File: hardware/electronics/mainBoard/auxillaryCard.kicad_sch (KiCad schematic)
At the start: 0 parts

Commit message: added sheet
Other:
- title: (none) -> EPS Controller
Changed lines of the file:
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@@
 	(generator "eeschema")
 	(generator_version "9.0")
-	(paper "A4")
+	(paper "USLetter")
 	(title_block
+		(title "EPS Controller")
+		(date "2025-02-26")
 		(rev "1")
 		(comment 2 "PROTOTYPE")

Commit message: renamed sheet
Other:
- title: EPS Controller -> Auxillary M.2 Card
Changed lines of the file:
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@@
 	(paper "USLetter")
 	(title_block
-		(title "EPS Controller")
-		(date "2025-02-26")
+		(title "Auxillary M.2 Card")
+		(date "2025-03-03")
 		(rev "1")
 		(comment 2 "PROTOTYPE")

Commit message: added aux card hardware
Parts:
- added C127, C129, C131, C134: 100nF, lib_fp:MLCC0603, symbol lib_sch:C
- added C128, C89: 1uF, symbol lib_sch:C
- added C130, C132, C133: 100nF, symbol lib_sch:C
- added D13, D16, D17: ~, symbol lib_sch:LED
- added J12: Bus_M.2_Socket_E, symbol lib_sch:Bus_M.2_Socket_E
- added J6: M.2 Standoff, symbol lib_sch:Mounting-Hole
- added R80, R81, R84: 100R, symbol lib_sch:R
- added R82: 10K, symbol lib_sch:R_horizontal
- added R83: VAL, symbol lib_sch:R_horizontal
- added SW11, SW12: VAL, symbol .DS-Switches:SPDT
- added U21: TPS22996H-Q1, symbol lib_sch:TPS22996H-Q1
- added U22: TXS0104VxRUTR, symbol lib_sch:TXS0108EQWRKSRQ1
- added U23: TXS0104VxRUTR, lib_fp:RUT0012A, symbol lib_sch:TXS0104VxRUTR
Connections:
- new net: C129.1, SW12.2, U23.1 (VCCA)
- new net: D13.2, R80.1
- new net: D17.2, R84.1
- new net: C127.1, SW11.2, U22.2 (VCCA)
- new net: D16.2, R81.1
- new net: C130.1, U21.8 (VBIAS)
- new net +1V8: C89.1, U21.3 (VIN2)
- new net +3V3: C128.1, U21.2 (VIN1)
- new net AUX.GPIO1: U23.10 (B1)
- new net AUX.GPIO2: U23.9 (B2)
- new net AUX.GPIO3: U23.8 (B3)
- new net AUX.PWR_EN: R82.1, R83.1
- new net AUX.RST: J12.52 (~{PERST0})
- new net AUX_1V8: C132.1, SW11.3, SW12.3, U21.6 (VOUT2), U22.10 (OE), U23.12 (OE)
- new net AUX_CTS_1V8: J12.34 (UART_CTS), U22.4 (A3)
- new net AUX_GPIO1_1V8: J12.38 (VENDOR_DEFINED), U23.2 (A1)
- new net AUX_GPIO2_1V8: J12.40 (VENDOR_DEFINED), U23.3 (A2)
- new net AUX_GPIO3_1V8: J12.42 (VENDOR_DEFINED), U23.4 (A3)
- new net AUX_LED1: D16.1, J12.6 (~{LED_1})
- new net AUX_LED2: D13.1, J12.16 (~{LED_2})
- new net AUX_RTS_1V8: J12.36 (UART_RTS), U22.5 (A4)
- new net AUX_RXD_1V8: J12.22 (UART_RXD), U22.1 (A1)
- new net AUX_SCL_1V8: J12.60 (I2C_CLK), U22.7 (A6)
- new net AUX_SDA_1V8: J12.58 (I2C_DATA), U22.6 (A5)
- new net AUX_TXD_1V8: J12.32 (UART_TXD), U22.3 (A2)
- new net AUX_VDD: C131.1, C133.1, C134.1, D17.1, J12.2 (3.3V), J12.4 (3.3V), J12.72 (3.3V), J12.74 (3.3V), SW11.1, SW12.1, U21.7 (VOUT1), U22.19 (VCCB), U23.11 (VCCB)
- new net HUSB3.DM: J12.5 (USB_D-)
- new net HUSB3.DP: J12.3 (USB_D+)
- new net I2C4.SDA: U22.15 (B5)
- new net I2C4SCL: U22.14 (B6)
- new net ON1: R82.2, U21.1 (ON1)
- new net ON2: R83.2, U21.4 (ON2)
- new net USART6.CTS: U22.17 (B3)
- new net USART6.RTS: U22.16 (B4)
- new net USART6.RX: U22.18 (B2)
- new net USART6.TX: U22.20 (B1)
- new net VSS: C127.2, C128.2, C129.2, C130.2, C131.2, C132.2, C133.2, C134.2, C89.2, J12.1 (GND), J12.18 (GND), J12.33 (GND), J12.39 (GND), J12.45 (GND), J12.51 (GND), J12.57 (GND), J12.63 (GND), J12.69 (GND), J12.7 (GND), J12.75 (GND), J6.1, R80.2, R81.2, R84.2, U21.5 (GND), U22.11 (GND), U22.21 (GND_Pad), U23.6 (GND)
- no-connect marks 0 -> 44
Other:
- note added: "GPIO Voltage Selection"
- note added: "I2C/USART Voltage Selection"

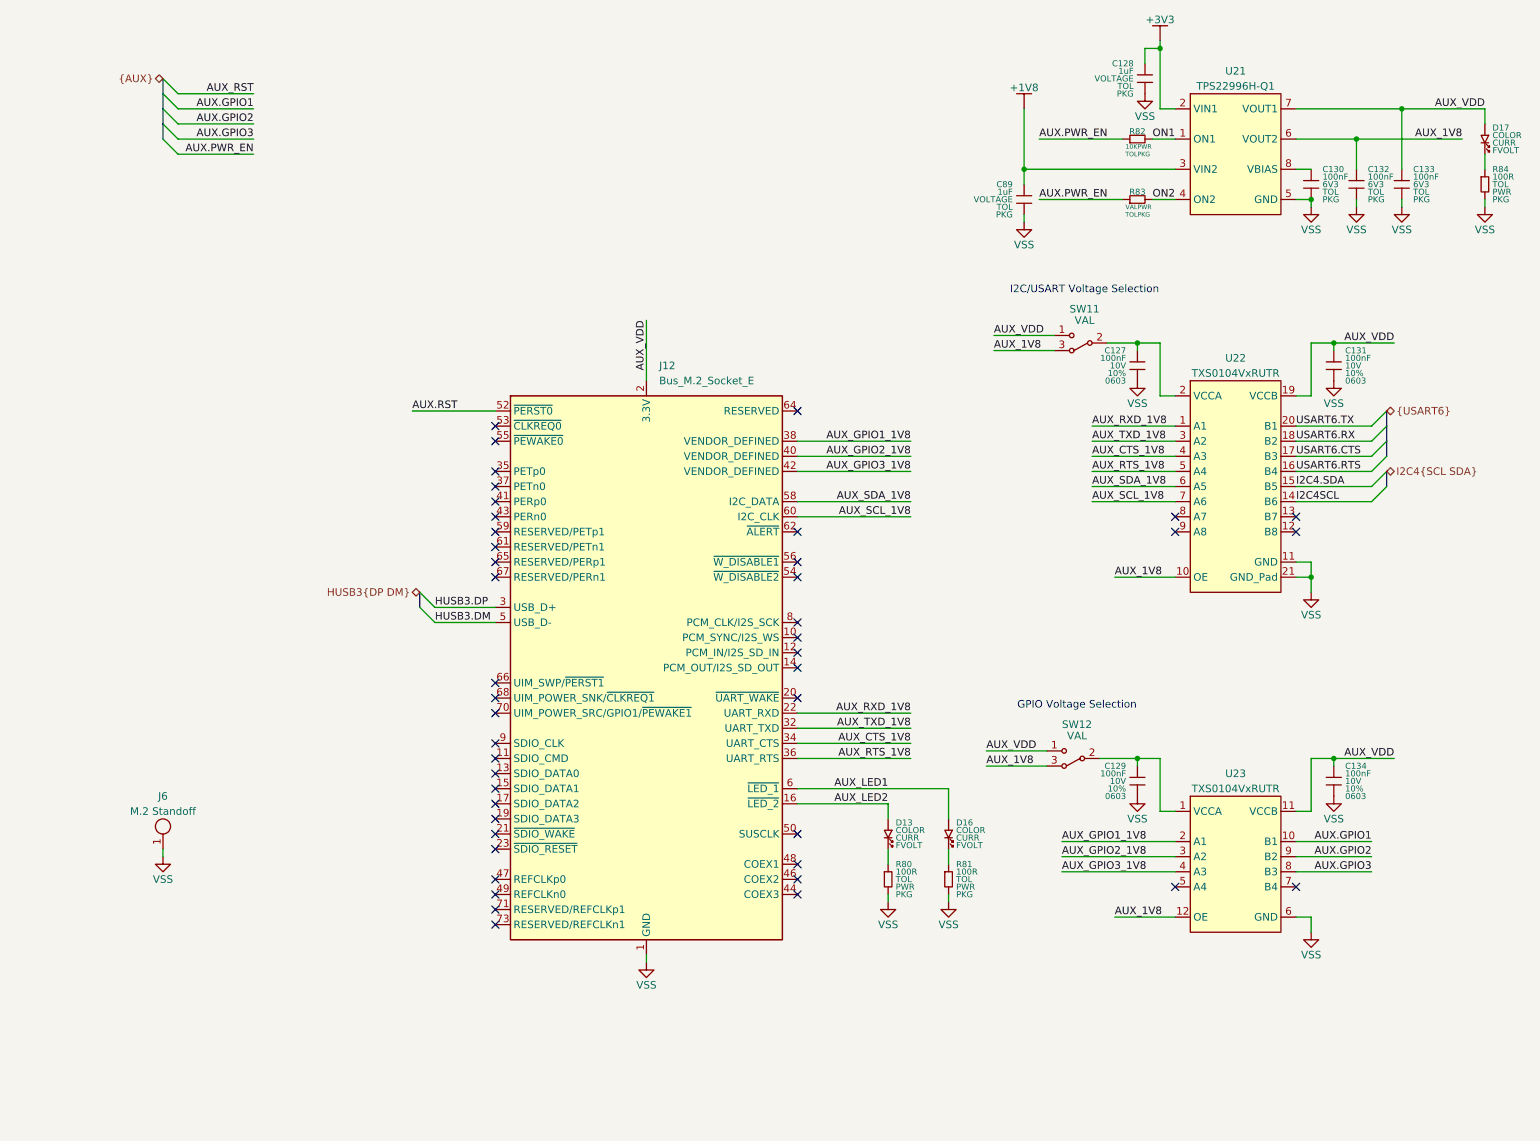
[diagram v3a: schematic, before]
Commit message: added components for aux card
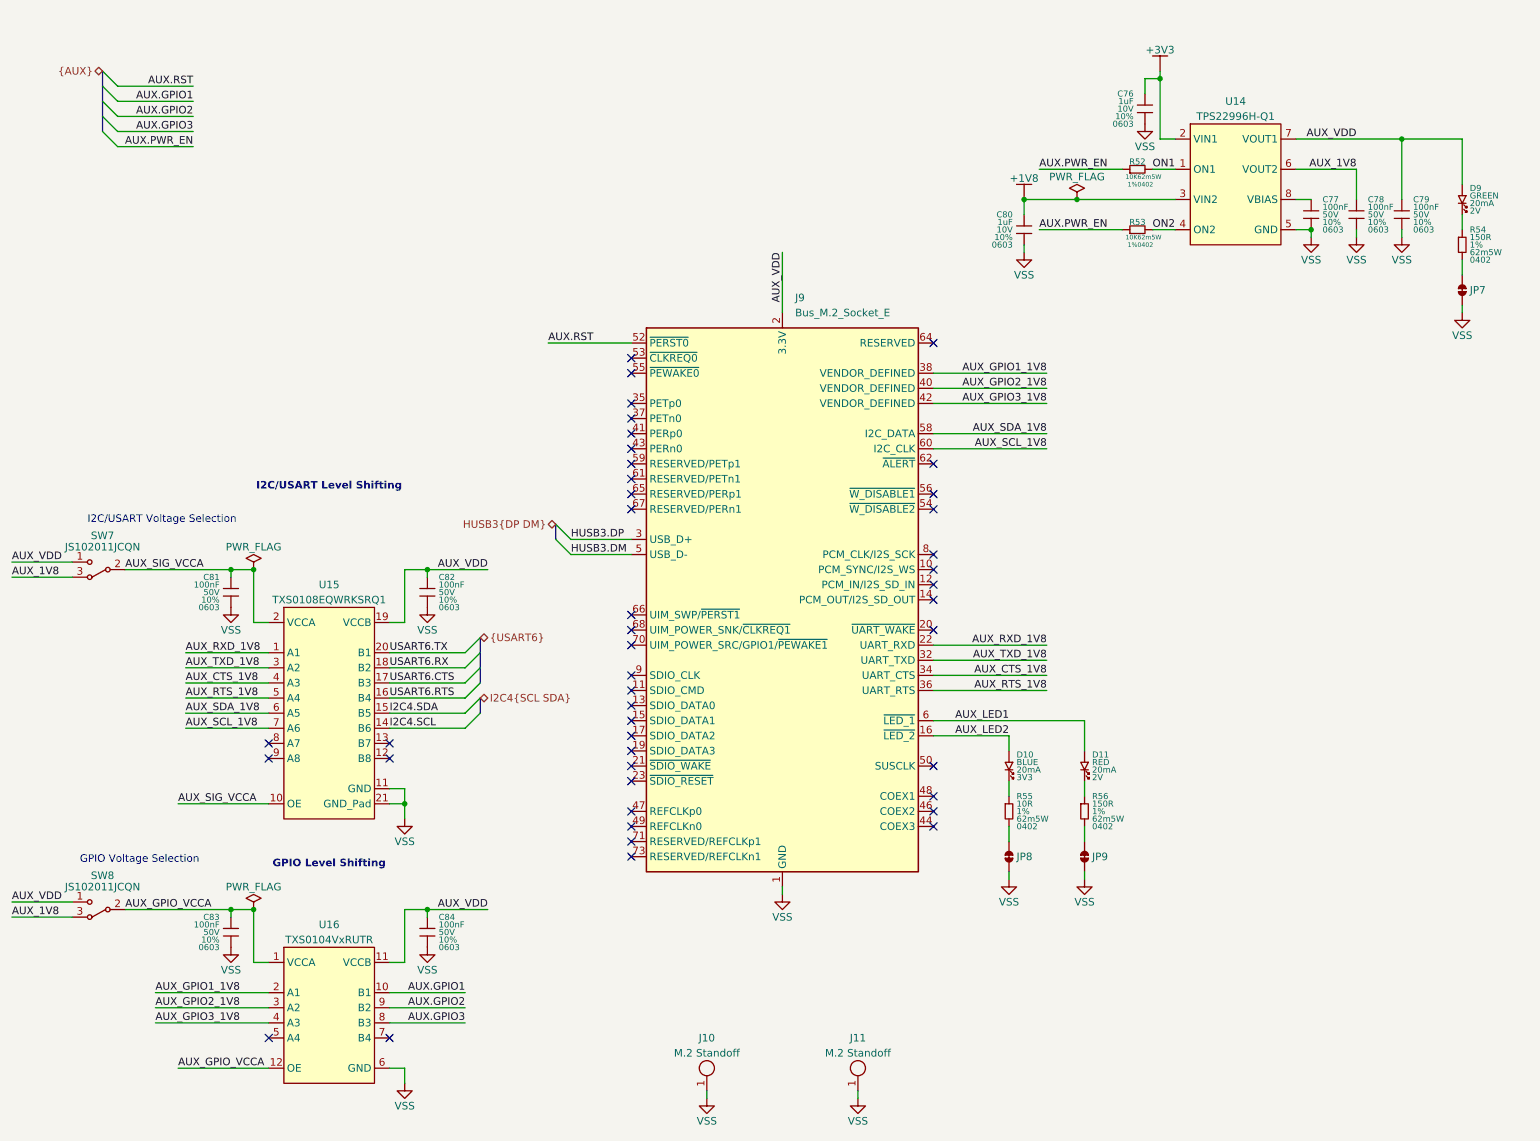
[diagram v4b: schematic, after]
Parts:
- removed C127, C129, C131, C134: 100nF, lib_fp:MLCC0603, symbol lib_sch:C
- removed C128, C89: 1uF, symbol lib_sch:C
- removed C130, C132, C133: 100nF, symbol lib_sch:C
- removed D13, D16, D17: ~, symbol lib_sch:LED
- removed J12: Bus_M.2_Socket_E, symbol lib_sch:Bus_M.2_Socket_E
- removed J6: M.2 Standoff, symbol lib_sch:Mounting-Hole
- removed R80, R81, R84: 100R, symbol lib_sch:R
- removed R82: 10K, symbol lib_sch:R_horizontal
- removed R83: VAL, symbol lib_sch:R_horizontal
- removed SW11, SW12: VAL, symbol .DS-Switches:SPDT
- removed U22: TXS0104VxRUTR, symbol lib_sch:TXS0108EQWRKSRQ1
- added C76, C80: 1uF, symbol lib_sch:C
- added C77, C78, C79, C81, C82, C83, C84: 100nF, symbol lib_sch:C
- added D10: LTST-C191TBKT, symbol lib_sch:LED
- added D11: LTST-C191KRKT, symbol lib_sch:LED
- added D9: LTST-C191KGKT, symbol lib_sch:LED
- added J10, J11: M.2 Standoff, symbol lib_sch:Mounting-Hole
- added J9: Bus_M.2_Socket_E, symbol lib_sch:Bus_M.2_Socket_E
- added JP7, JP8, JP9: ~, symbol lib_sch:Jumper_2_Bridged
- added R52, R53: 10K, symbol lib_sch:R_horizontal
- added R54, R56: 150R, symbol lib_sch:R
- added R55: 10R, symbol lib_sch:R
- added SW7, SW8: JS102011JCQN, symbol lib_sch:SPDT
- added U15: TXS0108EQWRKSRQ1, symbol lib_sch:TXS0108EQWRKSRQ1
- U16: renamed from U23; footprint lib_fp:RUT0012A -> (none)
- renumbered U21 to U14
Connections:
- net +1V8: now also C80.1
- net +3V3: now also C76.1
- net AUX.PWR_EN: now also R52.1, R53.1
- net AUX.RST: now also J9.52 (~{PERST0})
- net AUX_1V8: now also C78.1, SW7.3, SW8.3; no longer U16.12 (OE)
- net AUX_CTS_1V8: now also J9.34 (UART_CTS), U15.4 (A3)
- net AUX_GPIO1_1V8: now also J9.38 (VENDOR_DEFINED)
- net AUX_GPIO2_1V8: now also J9.40 (VENDOR_DEFINED)
- net AUX_GPIO3_1V8: now also J9.42 (VENDOR_DEFINED)
- net AUX_LED1: now also D11.1, J9.6 (~{LED_1})
- net AUX_LED2: now also D10.1, J9.16 (~{LED_2})
- net AUX_RTS_1V8: now also J9.36 (UART_RTS), U15.5 (A4)
- net AUX_RXD_1V8: now also J9.22 (UART_RXD), U15.1 (A1)
- net AUX_SCL_1V8: now also J9.60 (I2C_CLK), U15.7 (A6)
- net AUX_SDA_1V8: now also J9.58 (I2C_DATA), U15.6 (A5)
- net AUX_TXD_1V8: now also J9.32 (UART_TXD), U15.3 (A2)
- net AUX_VDD: now also C79.1, C82.1, C84.1, D9.1, J9.2 (3.3V), J9.4 (3.3V), J9.72 (3.3V), J9.74 (3.3V), SW7.1, SW8.1, U15.19 (VCCB)
- net HUSB3.DM: now also J9.5 (USB_D-)
- net HUSB3.DP: now also J9.3 (USB_D+)
- net I2C4.SDA: now also U15.15 (B5)
- net ON1: now also R52.2
- net ON2: now also R53.2
- net USART6.CTS: now also U15.17 (B3)
- net USART6.RTS: now also U15.16 (B4)
- net USART6.RX: now also U15.18 (B2)
- net USART6.TX: now also U15.20 (B1)
- net VSS: now also C76.2, C77.2, C78.2, C79.2, C80.2, C81.2, C82.2, C83.2, C84.2, J10.1, J11.1, J9.1 (GND), J9.18 (GND), J9.33 (GND), J9.39 (GND), J9.45 (GND), J9.51 (GND), J9.57 (GND), J9.63 (GND), J9.69 (GND), J9.7 (GND), J9.75 (GND), JP7.2, JP8.2, JP9.2, U15.11 (GND), U15.21 (GND_Pad)
- net AUX_GPIO_VCCA: now reaches U16.1 (VCCA)
- net AUX_GPIO_VCCA: now also U16.12 (OE), C83.1, SW8.2
- net at U14.8 (VBIAS): now also C77.1
- new net: D10.2, R55.1
- new net: JP8.1, R55.2
- new net: D9.2, R54.1
- new net: JP9.1, R56.2
- new net: JP7.1, R54.2
- new net: D11.2, R56.1
- new net AUX_SIG_VCCA: C81.1, SW7.2, U15.10 (OE), U15.2 (VCCA)
- new net I2C4.SCL: U15.14 (B6)
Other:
- note added: "GPIO Level Shifting"
- note added: "I2C/USART Level Shifting"
- moved on the sheet: U14, U16
